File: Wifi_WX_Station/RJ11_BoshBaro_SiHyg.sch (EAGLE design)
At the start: 11 parts, among them U1 AS5030

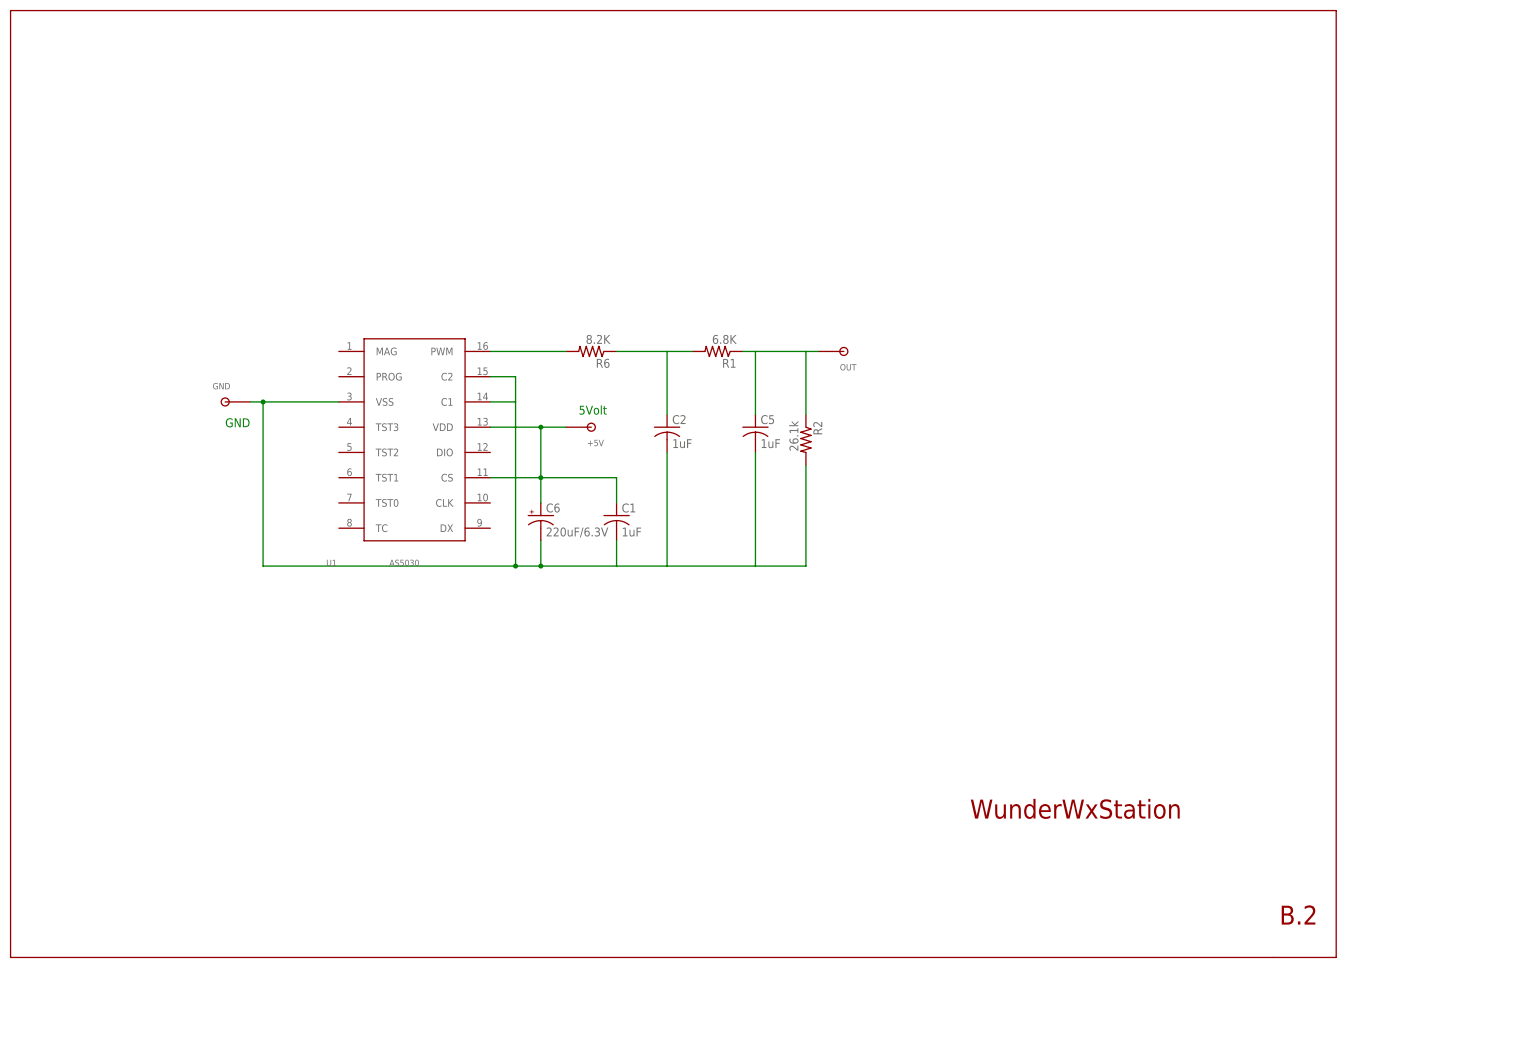
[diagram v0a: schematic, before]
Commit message: added SILabs Hygrometer board Added frames to the schematics
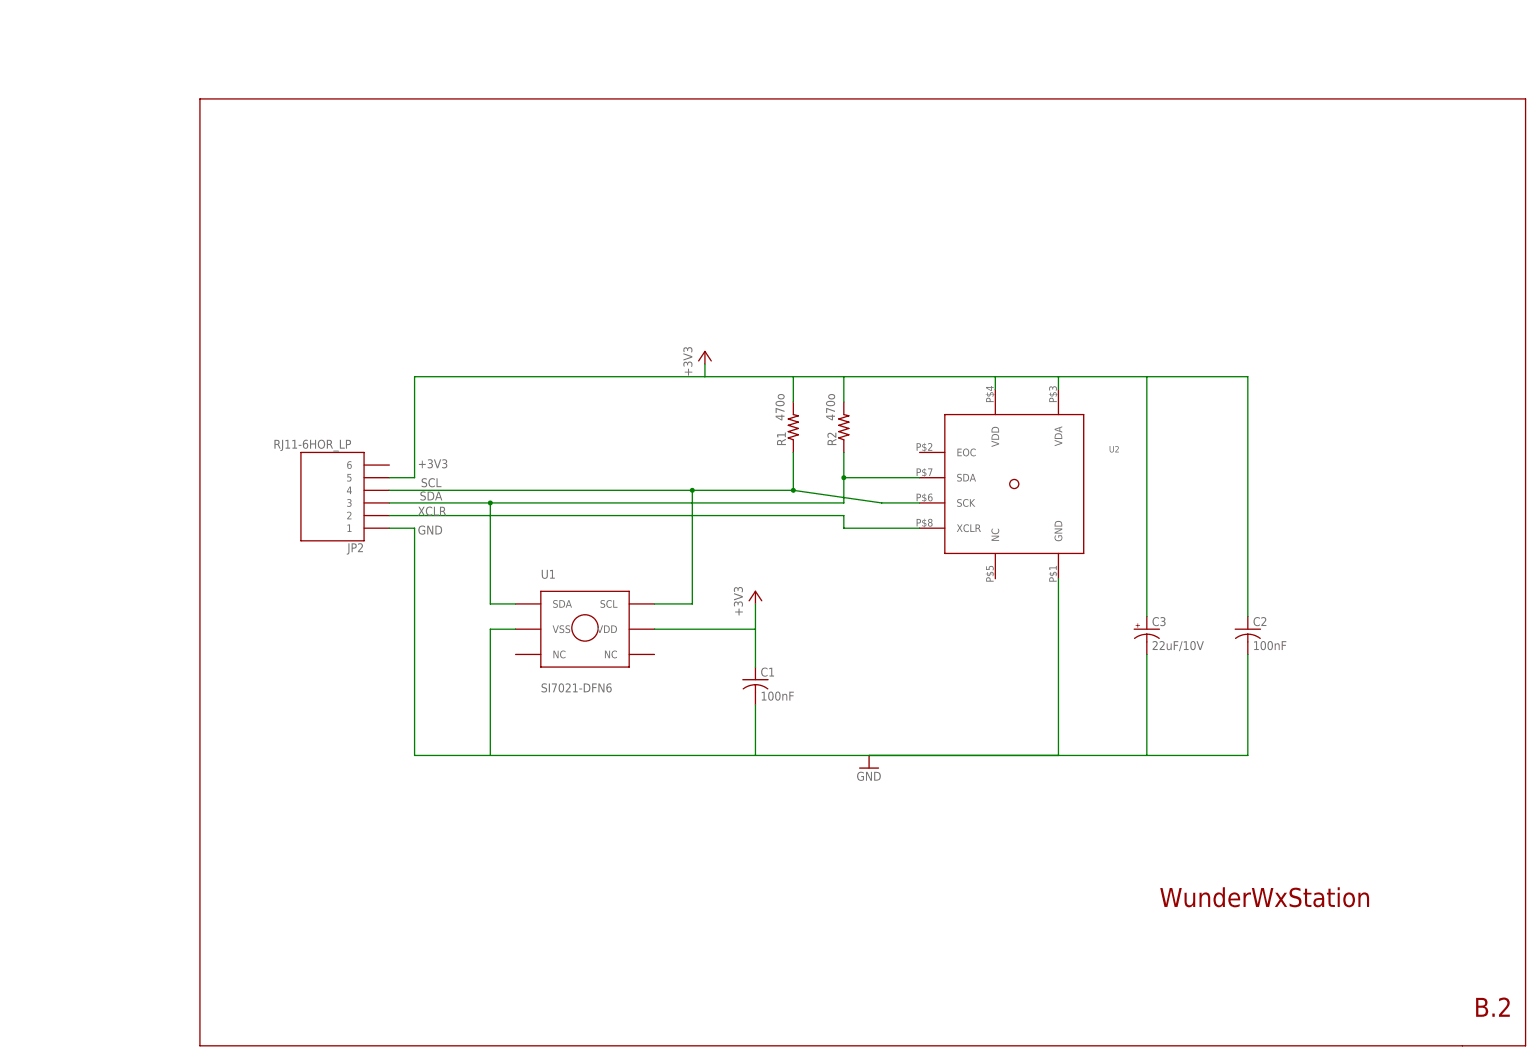
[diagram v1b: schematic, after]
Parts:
- removed +5V, GND, OUT: TPSOL, wifi_WX:TPSOL
- removed C5: 1uF, rcl:C-USC0805K
- removed C6: 220uF/6.3V, rcl:CPOL-USSMCD
- removed R6: 8.2K, rcl:R-US_R0603
- added C3: 22uF/10V, rcl:CPOL-USSMCB
- added JP2: RJ11-6HOR_LP, wifi_WX:RJ11-6HOR_LP
- added U2: (no value), 1AA_Stofer:BMP085
- C1, C2: value 1uF -> 100nF
- R1: value 6.8K -> 470o
- R2: value 26.1k -> 470o
- U1: value AS5030 -> SI7021-DFN6; device Stofer:AS5030 -> wifi_WX:SI7021-DFN6
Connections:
- removed net N$1: +5V.P$1, C1.1, C6.+, U1.CS, U1.VDD
- removed net N$2: C1.2, C2.2, C5.2, C6.-, GND.P$1, R2.2, U1.C1, U1.C2, U1.VSS
- removed net N$22: C2.1, R1.2, R6.1
- removed net N$23: R6.2, U1.PWM
- removed net N$3: C5.1, OUT.P$1, R1.1, R2.1
- new net +3V3: C1.1, C2.1, C3.+, JP2.5, R1.2, R2.2, U1.VDD, U2.VDA, U2.VDD
- new net GND: C1.2, C2.2, C3.-, JP2.1, U1.VSS, U2.GND
- new net SCL: JP2.4, R1.1, U1.SCL, U2.SCK
- new net SDA: JP2.3, R2.1, U1.SDA, U2.SDA
- new net XCLR: JP2.2, U2.XCLR
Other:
- note removed: "5Volt"
- note removed: "GND"
- moved on the sheet: C1, C2, R1, R2
